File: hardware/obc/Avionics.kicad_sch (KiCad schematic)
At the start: 47 parts, among them J101 Conn_02x20_Odd_Even, U101 MAX706RESA, U102 ATSAMD51J20A-AU, U103 BMI088, Y101 32.768kHz

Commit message: obc: final adjustments
Passed DRC, added board text, redid connector mechanicals, and routed highest current net.
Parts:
- L101: footprint SSE_Footprints:Sunlord_0805_3.0x3.0mm -> SSE_Footprints:L_Sunlord_2.0x1.6mm
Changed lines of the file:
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@@
 		(title "Obi Wan Computer")
 		(date "2024-06-07")
-		(rev "vA")
+		(rev "1")
 		(company "Ruchir Kavulli, Michael Lyle")
 		(comment 1 "Derived from PyCubed Mainboard v5")
@@
 			)
 		)
-		(property "Footprint" "SSE_Footprints:Sunlord_0805_3.0x3.0mm"
+		(property "Footprint" "SSE_Footprints:L_Sunlord_2.0x1.6mm"
 			(at 128.27 100.33 0)
 			(effects

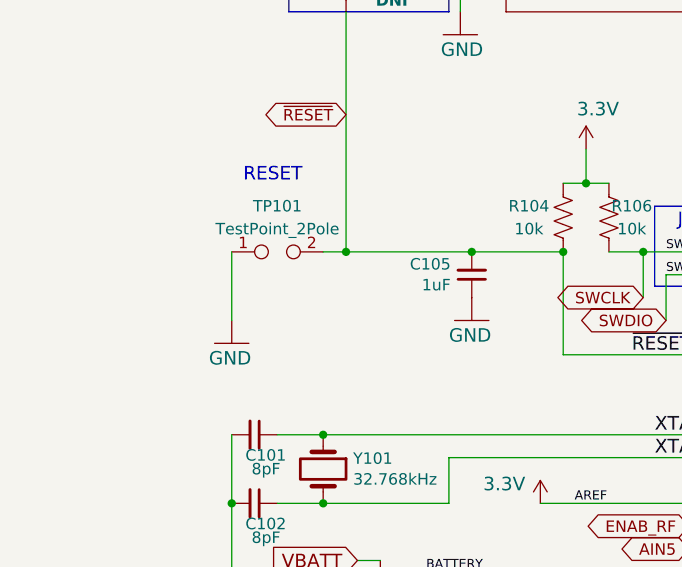
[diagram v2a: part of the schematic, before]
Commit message: obc: power path and routing changes
- Widen all the critical power paths
- Flip C416/R225 to improve routing
- Pin swap GND/GNDREF on RBF jumpers to improve routing
- Route USB D+/D- in differential fashion
- Correct schematic: test point that was removed was not removed
from schem.

Primary known TODO:

- Add more vias to critical power paths
- Route RF
- BOM fixes
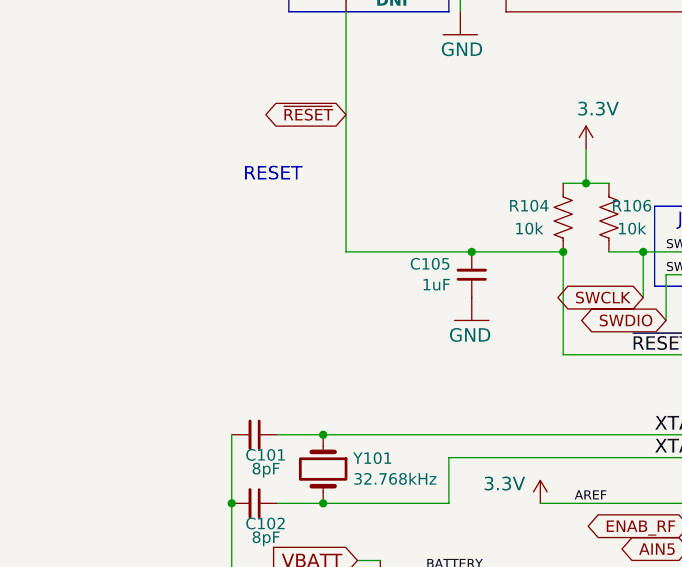
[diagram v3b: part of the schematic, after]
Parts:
- removed TP101: TestPoint_2Pole, TestPoint:TestPoint_2Pads_Pitch2.54mm_Drill0.8mm, symbol Connector:TestPoint_2Pole
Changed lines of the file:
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@@
 	)
 	(junction
-		(at 52.07 85.09)
-		(diameter 0)
-		(color 0 0 0 0)
-	)
-	(junction
 		(at 146.05 105.41)
 		(diameter 0)
@@
 	(wire
 		(pts
-			(xy 39.37 85.09) (xy 39.37 92.71)
-		)
-		(stroke
-			(width 0)
-			(type default)
-		)
-	)
-	(wire
-		(pts
 			(xy 66.04 85.09) (xy 76.2 85.09)
 		)
@@
 	(wire
 		(pts
-			(xy 49.53 85.09) (xy 52.07 85.09)
-		)
-		(stroke
-			(width 0)
-			(type default)
-		)
-	)
-	(wire
-		(pts
 			(xy 124.46 180.34) (xy 124.46 184.15)
 		)
@@
 	)
 	(symbol
-		(lib_id "mainboard:GND")
-		(at 39.37 95.25 0)
-		(unit 1)
-		(exclude_from_sim no)
-		(in_bom yes)
-		(on_board yes)
-		(dnp no)
-		(property "Reference" "#GND0101"
-			(at 39.37 95.25 0)
-			(effects
-				(font
-					(size 1.27 1.27)
-				)
-				(hide yes)
-			)
-		)
-		(property "Value" "GND"
-			(at 36.83 97.79 0)
-			(effects
-				(font
-					(size 1.4986 1.4986)
-				)
-				(justify left bottom)
-			)
-		)
-		(property "Footprint" ""
-			(at 39.37 95.25 0)
-			(effects
-				(font
-					(size 1.27 1.27)
-				)
-				(hide yes)
-			)
-		)
-		(property "Datasheet" ""
-			(at 39.37 95.25 0)
-			(effects
-				(font
-					(size 1.27 1.27)
-				)
-				(hide yes)
-			)
-		)
-		(property "Description" ""
-			(at 39.37 95.25 0)
-			(effects
-				(font
-					(size 1.27 1.27)
-				)
-				(hide yes)
-			)
-		)
-		(pin "1"
-		)
-		(instances
-			(project "mainboard"
-				(path "/e3ac22ea-6806-4807-a025-571315789c25/00000000-0000-0000-0000-00005cec5a72"
-					(reference "#GND0101")
-					(unit 1)
-				)
-			)
-		)
-	)
-	(symbol
 		(lib_id "mainboard:C_Small")
 		(at 60.96 132.08 0)
@@
 					(unit 1)
 				)
-			)
-		)
-	)
-	(symbol
-		(lib_id "Connector:TestPoint_2Pole")
-		(at 44.45 85.09 0)
-		(unit 1)
-		(exclude_from_sim no)
-		(in_bom yes)
-		(on_board yes)
-		(dnp no)
-		(fields_autoplaced yes)
-		(property "Reference" "TP101"
-			(at 44.45 80.01 0)
-			(effects
-				(font
-					(size 1.27 1.27)
-				)
-			)
-		)
-		(property "Value" "TestPoint_2Pole"
-			(at 44.45 82.55 0)
-			(effects
-				(font
-					(size 1.27 1.27)
-				)
-			)
-		)
-		(property "Footprint" "TestPoint:TestPoint_2Pads_Pitch2.54mm_Drill0.8mm"
-			(at 44.45 85.09 0)
-			(effects
-				(font
-					(size 1.27 1.27)
-				)
-				(hide yes)
-			)
-		)
-		(property "Datasheet" "~"
-			(at 44.45 85.09 0)
-			(effects
-				(font
-					(size 1.27 1.27)
-				)
-				(hide yes)
-			)
-		)
-		(property "Description" ""
-			(at 44.45 85.09 0)
-			(effects
-				(font
-					(size 1.27 1.27)
-				)
-				(hide yes)
-			)
-		)
-		(property "DNI" "DNI"
-			(at 44.45 85.09 0)
-			(effects
-				(font
-					(size 1.27 1.27)
-				)
-				(hide yes)
-			)
-		)
-		(property "Notes" ""
-			(at 44.45 85.09 0)
-			(effects
-				(font
-					(size 1.27 1.27)
-				)
-				(hide yes)
-			)
-		)
-		(property "Height" ""
-			(at 44.45 85.09 0)
-			(effects
-				(font
-					(size 1.27 1.27)
-				)
-				(hide yes)
-			)
-		)
-		(property "Mouser Part Number" ""
-			(at 44.45 85.09 0)
-			(effects
-				(font
-					(size 1.27 1.27)
-				)
-				(hide yes)
-			)
-		)
-		(property "Mouser Price/Stock" ""
-			(at 44.45 85.09 0)
-			(effects
-				(font
-					(size 1.27 1.27)
-				)
-				(hide yes)
-			)
-		)
-		(pin "2"
-		)
-		(pin "1"
-		)
-		(instances
-			(project "mainboard"
-				(path "/e3ac22ea-6806-4807-a025-571315789c25/00000000-0000-0000-0000-00005cec5a72"
-					(reference "TP101")
-					(unit 1)
-				)

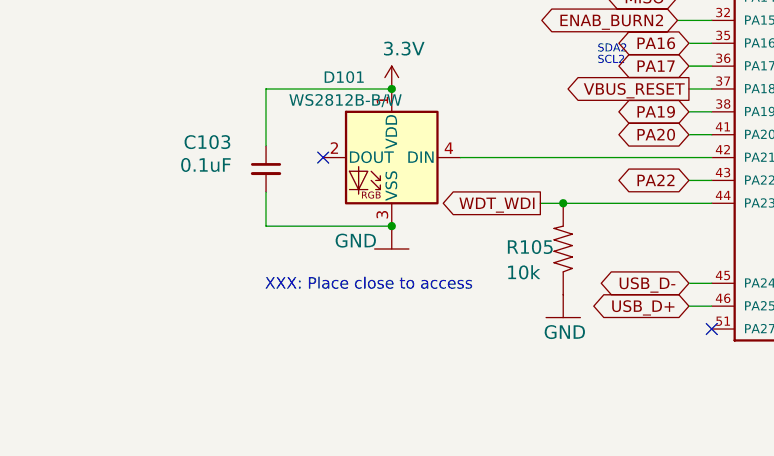
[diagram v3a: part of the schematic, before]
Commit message: obc: remove superfluous schem XXX comments
All were reviewed.

- Some didn't matter - entire comment removed
- Some were just notes, not action items - XXX notation removed

Two items noted do have implications, though:

- WDT rst pulldown value is incorrect.
- I2C pulls are missing (though this could be ignored).
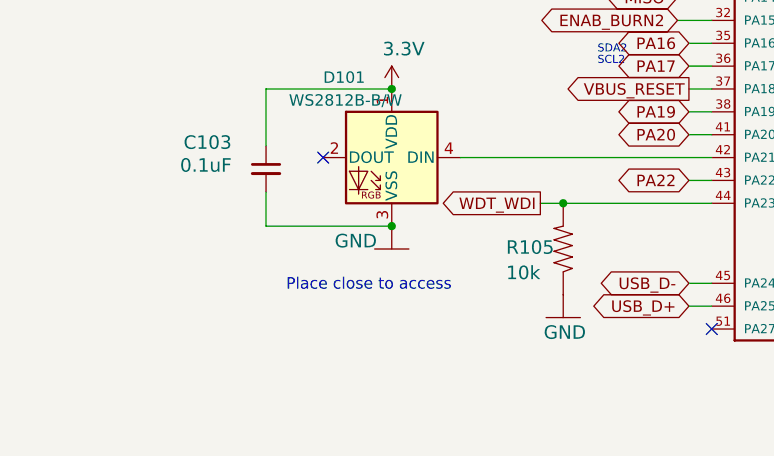
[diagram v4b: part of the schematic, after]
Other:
- note added: "Place close to access"
- note removed: "XXX: Place close to access"
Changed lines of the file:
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@@
 		)
 	)
-	(text "XXX: Place close to access"
+	(text "Place close to access"
 		(exclude_from_sim no)
 		(at 54.61 172.974 0)

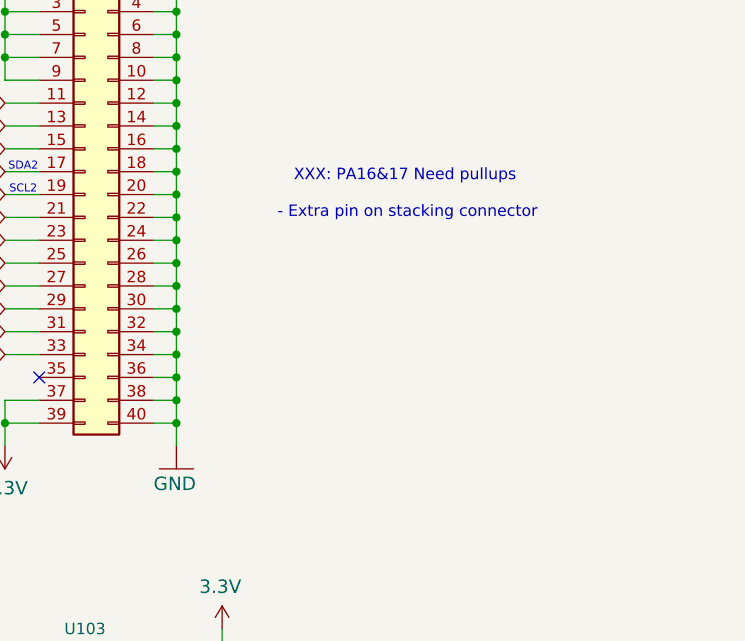
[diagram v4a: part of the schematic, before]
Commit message: obc: add I2C pullups of 1kohm for stacking bus
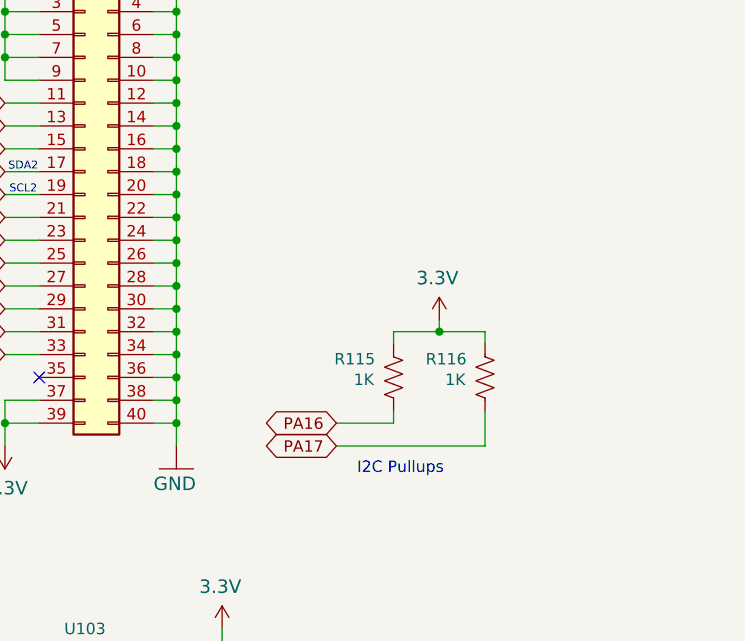
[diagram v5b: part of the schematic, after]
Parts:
- added R115, R116: 1K, Resistor_SMD:R_0603_1608Metric, symbol Device:R_US
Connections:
- net 3.3V: now also R115.1, R116.1
- net PA16: now also R115.2
- net PA17: now also R116.2
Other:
- note added: "I2C Pullups"
- note removed: "XXX: PA16&17 Need pullups - Extra pin on stacking connector"

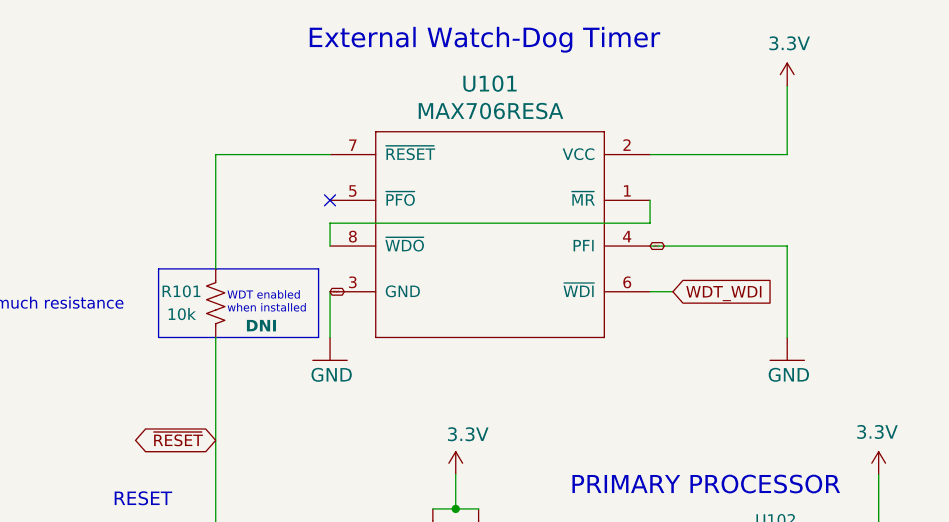
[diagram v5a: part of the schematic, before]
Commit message: obc: corrections to watchdog circuit
Per MAX706 datasheet, tie MR# high instead of to WDO#.

Also, use a 680 ohm resistor to drive microcontroller RST#
signal; the original design was a 10k/10k divider which would
have put it midrail; this will swing 95% of the way now and
should be good enough.
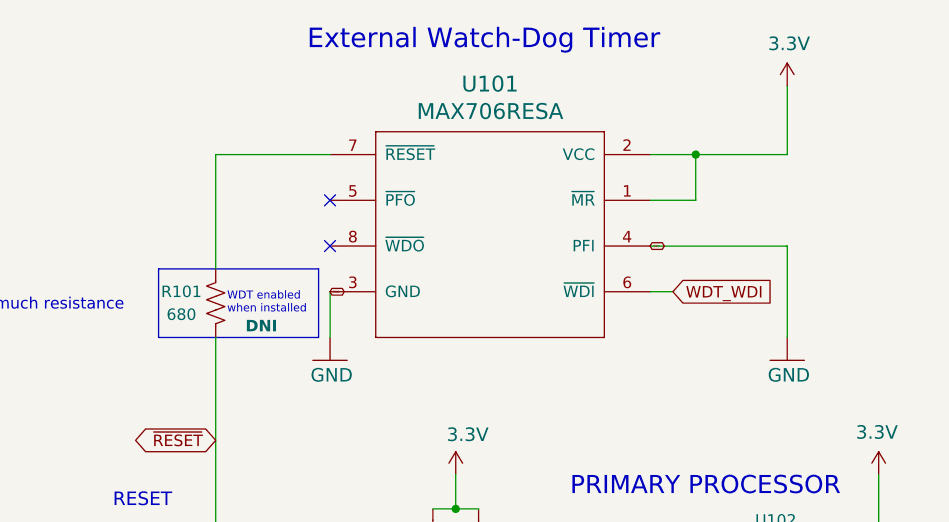
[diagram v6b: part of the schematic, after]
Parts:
- R101: value 10k -> 680; LCSC C169849 -> (none); Manufacturer_Name PANASONIC -> (none); Manufacturer_Part_Number ERJ3GEYJ103V -> (none)
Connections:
- net 3.3V: now also U101.1 (~{MR})
- net at U101.8 (~{WDO}): no longer U101.1 (~{MR})
- no-connect marks 13 -> 14
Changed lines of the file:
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@@
 	)
 	(junction
+		(at 105.41 38.1)
+		(diameter 0)
+		(color 0 0 0 0)
+	)
+	(junction
 		(at 151.13 85.09)
 		(diameter 0)
@@
 	)
 	(no_connect
+		(at 64.77 48.26)
+	)
+	(no_connect
 		(at 204.47 91.44)
 	)
@@
 	(wire
 		(pts
+			(xy 105.41 38.1) (xy 100.33 38.1)
+		)
+		(stroke
+			(width 0)
+			(type default)
+		)
+	)
+	(wire
+		(pts
 			(xy 49.53 113.03) (xy 63.5 113.03)
 		)
@@
 	(wire
 		(pts
-			(xy 64.77 48.26) (xy 64.77 45.72)
-		)
-		(stroke
-			(width 0)
-			(type default)
-		)
-	)
-	(wire
-		(pts
-			(xy 100.33 45.72) (xy 100.33 43.18)
+			(xy 100.33 43.18) (xy 105.41 43.18)
 		)
 		(stroke
@@
 	(wire
 		(pts
-			(xy 115.57 38.1) (xy 100.33 38.1)
+			(xy 115.57 38.1) (xy 105.41 38.1)
 		)
 		(stroke
@@
 	(wire
 		(pts
-			(xy 64.77 45.72) (xy 100.33 45.72)
-		)
-		(stroke
-			(width 0)
-			(type default)
-		)
-	)
-	(wire
-		(pts
 			(xy 135.89 90.17) (xy 135.89 92.71)
 		)
@@
 	(wire
 		(pts
+			(xy 105.41 43.18) (xy 105.41 38.1)
+		)
+		(stroke
+			(width 0)
+			(type default)
+		)
+	)
+	(wire
+		(pts
 			(xy 88.9 140.97) (xy 92.71 140.97)
 		)
@@
 			)
 		)
-		(property "Value" "10k"
+		(property "Value" "680"
 			(at 48.26 55.88 0)
 			(effects
@@
 			)
 		)
-		(property "Description" "10k 0603"
+		(property "Description" "680 0603"
 			(at 48.26 55.88 0)
 			(effects
@@
 			)
 		)
-		(property "LCSC" "C169849"
+		(property "LCSC" ""
 			(at 52.07 54.61 0)
 			(effects
@@
 			)
 		)
-		(property "Manufacturer_Name" "PANASONIC"
+		(property "Manufacturer_Name" ""
 			(at 52.07 54.61 0)
 			(effects
@@
 			)
 		)
-		(property "Manufacturer_Part_Number" "ERJ3GEYJ103V"
+		(property "Manufacturer_Part_Number" ""
 			(at 52.07 54.61 0)
 			(effects

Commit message: obc: adjust part numbers for resistors
Many of selected variants are difficult to source for assembly.
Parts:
- R102: LCSC C844550 -> C25814; Manufacturer_Name Vishay Intertech -> (none); Manufacturer_Part_Number CRCW0603316KFKEA -> (none)
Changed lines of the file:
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@@
 			)
 		)
-		(property "LCSC" "C844550"
+		(property "LCSC" "C25814"
 			(at 55.88 123.19 0)
 			(effects
@@
 			)
 		)
-		(property "Manufacturer_Name" " Vishay Intertech"
+		(property "Manufacturer_Name" ""
 			(at 55.88 123.19 0)
 			(effects
@@
 			)
 		)
-		(property "Manufacturer_Part_Number" " CRCW0603316KFKEA"
+		(property "Manufacturer_Part_Number" ""
 			(at 55.88 123.19 0)
 			(effects

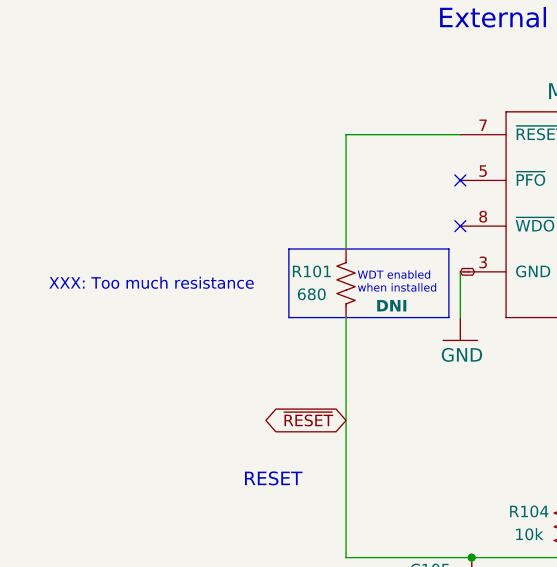
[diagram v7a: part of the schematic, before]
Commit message: obc: remove errant "too much resistance" comment
Was fixed in d3ba5395cb556b76f2be0f4a4653125f56a0b98e .
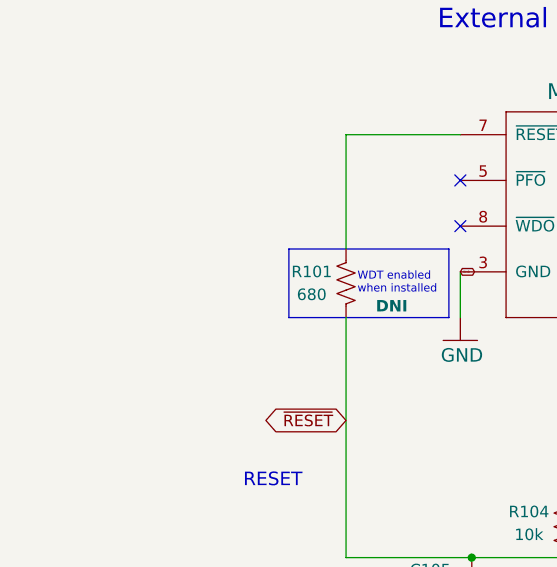
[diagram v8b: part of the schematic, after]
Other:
- note removed: "XXX: Too much resistance"
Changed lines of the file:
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@@
-		)
-	)
-	(text "XXX: Too much resistance"
-		(exclude_from_sim no)
-		(at 30.48 54.864 0)
-		(effects
-			(font
-				(size 1.27 1.27)
-			)
 		)
 	)
